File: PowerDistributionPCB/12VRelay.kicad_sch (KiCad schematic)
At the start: 1 part

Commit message: updated relays
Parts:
- removed K?: 5V Relay, ORWH-SH-105D1F_000:RELAY_ORWH-SH-105D1F_000, symbol Relays:ORWH-SH-105D1F_000
- added 12VRelay?: AZ943-1CH-12DE, AZ943-1CH_AMZ, symbol Relays:AZ943-1CH-12DE
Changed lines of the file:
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@@
 	(generator_version "9.0")
 	(paper "A4")
-	(hierarchical_label "PicoConnection"
+	(hierarchical_label "VCC"
 		(shape input)
-		(at 184.15 62.23 0)
+		(at 165.1 68.58 0)
 		(effects
 			(font
@@
 	(hierarchical_label "VIN"
 		(shape input)
-		(at 184.15 54.61 0)
+		(at 165.1 64.77 0)
 		(effects
 			(font
@@
 		)
 	)
-	(hierarchical_label "VCC"
+	(hierarchical_label "PicoConnection"
 		(shape input)
-		(at 184.15 58.42 0)
+		(at 165.1 72.39 0)
 		(effects
 			(font
@@
 	(hierarchical_label "Out"
 		(shape output)
-		(at 184.15 50.8 0)
+		(at 165.1 60.96 0)
 		(effects
 			(font
@@
 	)
 	(symbol
-		(lib_id "Relays:ORWH-SH-105D1F_000")
-		(at 120.65 62.23 0)
+		(lib_id "Relays:AZ943-1CH-12DE")
+		(at 120.65 63.5 0)
 		(unit 1)
 		(exclude_from_sim no)
@@
 		(dnp no)
 		(fields_autoplaced yes)
-		(property "Reference" "K?"
-			(at 120.65 52.07 0)
+		(property "Reference" "12VRelay?"
+			(at 135.89 55.88 0)
+			(effects
+				(font
+					(size 1.524 1.524)
+				)
+			)
+		)
+		(property "Value" "AZ943-1CH-12DE"
+			(at 135.89 58.42 0)
+			(effects
+				(font
+					(size 1.524 1.524)
+				)
+			)
+		)
+		(property "Footprint" "AZ943-1CH_AMZ"
+			(at 120.65 63.5 0)
 			(effects
 				(font
 					(size 1.27 1.27)
+					(italic yes)
 				)
+				(hide yes)
 			)
 		)
-		(property "Value" "5V Relay"
-			(at 120.65 54.61 0)
+		(property "Datasheet" "AZ943-1CH-12DE"
+			(at 120.65 63.5 0)
 			(effects
 				(font
 					(size 1.27 1.27)
+					(italic yes)
 				)
-			)
-		)
-		(property "Footprint" "ORWH-SH-105D1F_000:RELAY_ORWH-SH-105D1F_000"
-			(at 120.65 62.23 0)
-			(effects
-				(font
-					(size 1.27 1.27)
-				)
-				(justify bottom)
 				(hide yes)
 			)
 		)
-		(property "Datasheet" ""
-			(at 120.65 62.23 0)
+		(property "Description" ""
+			(at 120.65 63.5 0)
 			(effects
 				(font
@@
 			)
 		)
-		(property "Description" ""
-			(at 120.65 62.23 0)
-			(effects
-				(font
-					(size 1.27 1.27)
-				)
-				(hide yes)
-			)
-		)
-		(property "PARTREV" "D"
-			(at 120.65 62.23 0)
-			(effects
-				(font
-					(size 1.27 1.27)
-				)
-				(justify bottom)
-				(hide yes)
-			)
-		)
-		(property "STANDARD" "Manufacturer Recommendations"
-			(at 120.65 62.23 0)
-			(effects
-				(font
-					(size 1.27 1.27)
-				)
-				(justify bottom)
-				(hide yes)
-			)
-		)
-		(property "MAXIMUM_PACKAGE_HEIGHT" "16.3mm"
-			(at 120.65 62.23 0)
-			(effects
-				(font
-					(size 1.27 1.27)
-				)
-				(justify bottom)
-				(hide yes)
-			)
-		)
-		(property "MANUFACTURER" "TE Connectivity"
-			(at 120.65 62.23 0)
-			(effects
-				(font
-					(size 1.27 1.27)
-				)
-				(justify bottom)
-				(hide yes)
-			)
-		)
 		(pin "1"
 		)
 		(pin "2"
 		)
-		(pin "3"
+		(pin "5"
 		)
 		(pin "4"
 		)
-		(pin "5"
+		(pin "3"
 		)
 		(instances
 			(project ""
-				(path "/b27c75df-6223-4cc6-be69-062c2b02d5c6/bfd015dc-a1f5-42ba-b972-f7703fed8888"
-					(reference "K?")
+				(path "/b27c75df-6223-4cc6-be69-062c2b02d5c6/2554d0a8-0302-45bf-85e0-44db6e8d016e"
+					(reference "12VRelay?")
 					(unit 1)
 				)
@@
 	(symbol
 		(lib_id "power:GND")
-		(at 177.8 69.85 0)
+		(at 158.75 80.01 0)
 		(unit 1)
 		(exclude_from_sim no)
@@
 		(dnp no)
 		(fields_autoplaced yes)
-		(property "Reference" "#PWR?"
-			(at 177.8 76.2 0)
+		(property "Reference" "#PWR010"
+			(at 158.75 86.36 0)
 			(effects
 				(font
@@
 		)
 		(property "Value" "GND"
-			(at 177.8 74.93 0)
+			(at 158.75 85.09 0)
 			(effects
 				(font
@@
 		)
 		(property "Footprint" ""
-			(at 177.8 69.85 0)
+			(at 158.75 80.01 0)
 			(effects
 				(font
@@
 		)
 		(property "Datasheet" ""
-			(at 177.8 69.85 0)
+			(at 158.75 80.01 0)
 			(effects
 				(font
@@
 		)
 		(property "Description" "Power symbol creates a global label with name \"GND\" , ground"
-			(at 177.8 69.85 0)
+			(at 158.75 80.01 0)
 			(effects
 				(font
@@
 		(instances
 			(project "PowerDistributionPCB"
-				(path "/b27c75df-6223-4cc6-be69-062c2b02d5c6/4aa10ec7-4b36-4cde-a760-c4500e70a751"
-					(reference "#PWR01")
+				(path "/b27c75df-6223-4cc6-be69-062c2b02d5c6/2554d0a8-0302-45bf-85e0-44db6e8d016e"
+					(reference "#PWR010")
 					(unit 1)
 				)
-				(path "/b27c75df-6223-4cc6-be69-062c2b02d5c6/bfd015dc-a1f5-42ba-b972-f7703fed8888"
-					(reference "#PWR?")
-					(unit 1)
-				)

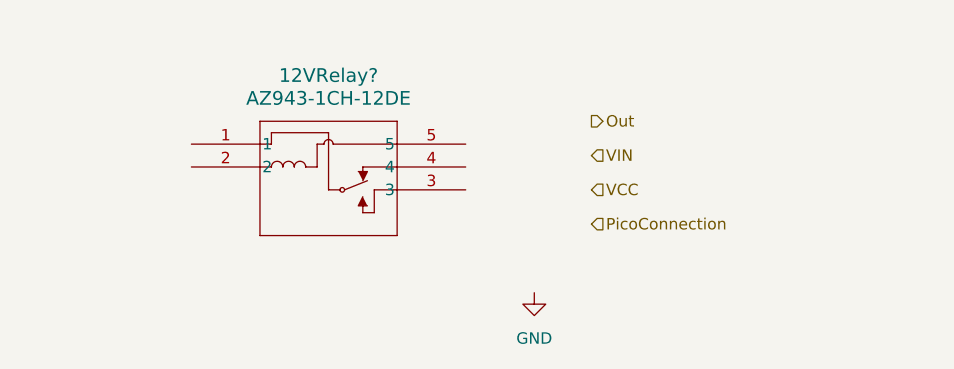
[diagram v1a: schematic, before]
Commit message: added relay connections
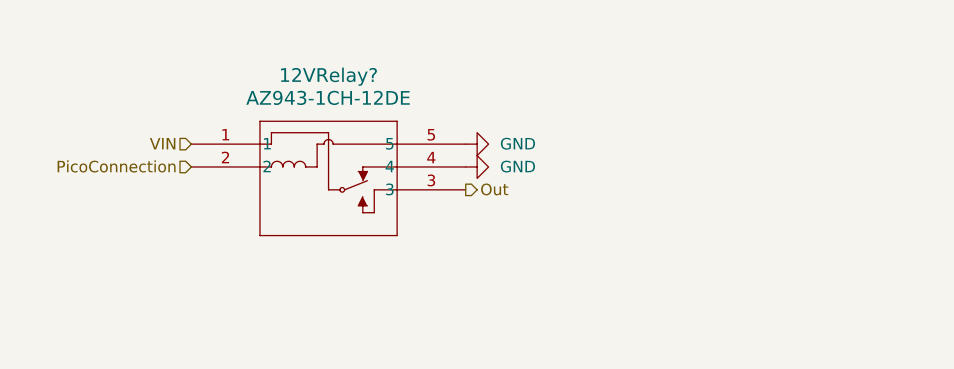
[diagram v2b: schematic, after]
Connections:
- net GND: now also 12VRelay?.4, 12VRelay?.5
- net Out: now also 12VRelay?.3
- net PicoConnection: now also 12VRelay?.2
- net VIN: now also 12VRelay?.1
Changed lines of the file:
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@@
 	(generator_version "9.0")
 	(paper "A4")
-	(hierarchical_label "VCC"
+	(hierarchical_label "VIN"
 		(shape input)
-		(at 165.1 68.58 0)
+		(at 120.65 63.5 180)
 		(effects
 			(font
 				(size 1.27 1.27)
 			)
-			(justify left)
-		)
-	)
-	(hierarchical_label "VIN"
+			(justify right)
+		)
+	)
+	(hierarchical_label "PicoConnection"
 		(shape input)
-		(at 165.1 64.77 0)
+		(at 120.65 66.04 180)
 		(effects
 			(font
 				(size 1.27 1.27)
 			)
-			(justify left)
-		)
-	)
-	(hierarchical_label "PicoConnection"
-		(shape input)
-		(at 165.1 72.39 0)
+			(justify right)
+		)
+	)
+	(hierarchical_label "Out"
+		(shape output)
+		(at 151.13 68.58 0)
 		(effects
 			(font
@@
 		)
 	)
-	(hierarchical_label "Out"
-		(shape output)
-		(at 165.1 60.96 0)
-		(effects
-			(font
-				(size 1.27 1.27)
-			)
-			(justify left)
+	(symbol
+		(lib_id "power:GND")
+		(at 151.13 66.04 90)
+		(unit 1)
+		(exclude_from_sim no)
+		(in_bom yes)
+		(on_board yes)
+		(dnp no)
+		(fields_autoplaced yes)
+		(property "Reference" "#PWR012"
+			(at 157.48 66.04 0)
+			(effects
+				(font
+					(size 1.27 1.27)
+				)
+				(hide yes)
+			)
+		)
+		(property "Value" "GND"
+			(at 154.94 66.0399 90)
+			(effects
+				(font
+					(size 1.27 1.27)
+				)
+				(justify right)
+			)
+		)
+		(property "Footprint" ""
+			(at 151.13 66.04 0)
+			(effects
+				(font
+					(size 1.27 1.27)
+				)
+				(hide yes)
+			)
+		)
+		(property "Datasheet" ""
+			(at 151.13 66.04 0)
+			(effects
+				(font
+					(size 1.27 1.27)
+				)
+				(hide yes)
+			)
+		)
+		(property "Description" "Power symbol creates a global label with name \"GND\" , ground"
+			(at 151.13 66.04 0)
+			(effects
+				(font
+					(size 1.27 1.27)
+				)
+				(hide yes)
+			)
+		)
+		(pin "1"
+		)
+		(instances
+			(project "PowerDistributionPCB"
+				(path "/b27c75df-6223-4cc6-be69-062c2b02d5c6/2554d0a8-0302-45bf-85e0-44db6e8d016e"
+					(reference "#PWR012")
+					(unit 1)
+				)
+			)
 		)
 	)
@@
 	(symbol
 		(lib_id "power:GND")
-		(at 158.75 80.01 0)
+		(at 151.13 63.5 90)
 		(unit 1)
 		(exclude_from_sim no)
@@
 		(fields_autoplaced yes)
 		(property "Reference" "#PWR010"
-			(at 158.75 86.36 0)
+			(at 157.48 63.5 0)
 			(effects
 				(font
@@
 		)
 		(property "Value" "GND"
-			(at 158.75 85.09 0)
-			(effects
-				(font
-					(size 1.27 1.27)
-				)
+			(at 154.94 63.4999 90)
+			(effects
+				(font
+					(size 1.27 1.27)
+				)
+				(justify right)
 			)
 		)
 		(property "Footprint" ""
-			(at 158.75 80.01 0)
+			(at 151.13 63.5 0)
 			(effects
 				(font
@@
 		)
 		(property "Datasheet" ""
-			(at 158.75 80.01 0)
+			(at 151.13 63.5 0)
 			(effects
 				(font
@@
 		)
 		(property "Description" "Power symbol creates a global label with name \"GND\" , ground"
-			(at 158.75 80.01 0)
-			(effects
-				(font
+			(at 151.13 63.5 0)
+			(effects
+				(font
